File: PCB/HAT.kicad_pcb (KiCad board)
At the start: 2 copper layers, 99.4 x 99 mm, 103 parts, among them J1 Conn_01x02_Pin, J10 Conn_01x24_Socket, J11 Conn_01x24_Pin, J12 Conn_01x02_Pin, J13 Conn_01x02_Pin, J14 Conn_01x02_Pin, J15 Conn_01x02_Pin, J2 Conn_01x02_Pin, J3 Conn_01x01_Pin, J4 Conn_01x02_Pin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

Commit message: fixing of PCB Design
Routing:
- net GND: track 120.5 -> 126.1 mm
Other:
- board size 99.4 x 99 mm -> 99.3 x 98.9 mm
- board text added: "CHARGING MODULE"
- board text added: "CLOCK GENERATOR"
- board text added: "EEEPROM"
- board text added: "FTDI"
- board text added: "POLARITY PROTECTION + UVLO"
- board text added: "PROXIMITY SENSOR"
- board text added: "SHIFTER GPIO0"
- board text added: "SHIFTER GPIO1"
- board text added: "SHIFTER SCL"
- board text added: "SHIFTER SDA"
- board text added: "USB-B"
- board text added: "V REG"
- board text added: "VOLT REG SENSE"
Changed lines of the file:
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@@
         (effects (font (size 1 1) (thickness 0.15)))
     )
-    (fp_text user "REF**" (at 0 4.8 180) (layer "F.Fab")
-        (effects (font (size 1 1) (thickness 0.15)))
-    )
     (fp_line (start -0.9 -0.8) (end 0.9 -0.8)
-      (stroke (width 0.254001) (type solid)) (layer "F.SilkS"))
+      (stroke (width 0.254) (type solid)) (layer "F.SilkS"))
     (fp_line (start -0.878105 0.8) (end 0.878105 0.8)
-      (stroke (width 0.254001) (type solid)) (layer "F.SilkS"))
+      (stroke (width 0.254) (type solid)) (layer "F.SilkS"))
     (fp_line (start -0.609601 0) (end 0.685801 0)
       (stroke (width 0.2) (type solid)) (layer "F.SilkS"))
@@
     (fp_arc (start 1.080188 -0.709627) (mid 1.299286 -0.618875) (end 1.390018 -0.399772)
       (stroke (width 0.254) (type solid)) (layer "F.SilkS"))
-    (fp_arc (start 1.390018 0.400203) (mid 1.299269 0.61928) (end 1.080188 0.710033)
+    (fp_arc (start 1.390018 0.400203) (mid 1.299267 0.619284) (end 1.080188 0.710033)
       (stroke (width 0.254) (type solid)) (layer "F.SilkS"))
     (fp_circle (center -0.800102 0.400051) (end -0.77013 0.400051)
@@
     (fp_arc (start 1.080188 -0.709627) (mid 1.299286 -0.618875) (end 1.390018 -0.399772)
       (stroke (width 0.254) (type solid)) (layer "F.SilkS"))
-    (fp_arc (start 1.390018 0.400203) (mid 1.299269 0.61928) (end 1.080188 0.710033)
+    (fp_arc (start 1.390018 0.400203) (mid 1.299267 0.619284) (end 1.080188 0.710033)
       (stroke (width 0.254) (type solid)) (layer "F.SilkS"))
     (fp_circle (center -0.800102 0.400051) (end -0.77013 0.400051)
@@
     )
   )
-  (gr_rect (start 96.5964 46.9657) (end 195.5964 145.6449)
-    (stroke (width 0.2) (type default)) (fill none) (layer "F.Cu"))
+  (gr_circle (center 137.3378 101.6762) (end 137.5156 101.854)
+    (stroke (width 0.15) (type default)) (fill solid) (layer "F.SilkS"))
   (gr_rect (start 123.5964 68.6449) (end 172.6164 86.5999)
     (stroke (width 0.15) (type default)) (fill none) (layer "F.SilkS"))
@@
   (gr_rect (start 142.3964 115.069824) (end 157.2964 144.019824)
     (stroke (width 0.15) (type default)) (fill none) (layer "F.SilkS"))
+  (gr_circle (center 101.967847 69.8349) (end 102.145647 70.0127)
+    (stroke (width 0.15) (type default)) (fill solid) (layer "F.SilkS"))
   (gr_rect (start 173.0864 68.6449) (end 188.1064 86.5999)
     (stroke (width 0.15) (type default)) (fill none) (layer "F.SilkS"))
+  (gr_circle (center 172.443153 100.7872) (end 172.620953 100.965)
+    (stroke (width 0.15) (type default)) (fill solid) (layer "F.SilkS"))
   (gr_line (start 98.7964 129.6699) (end 113.6964 129.6699)
     (stroke (width 0.15) (type default)) (layer "F.SilkS"))
   (gr_rect (start 97.5964 68.6449) (end 122.6164 86.5999)
     (stroke (width 0.15) (type default)) (fill none) (layer "F.SilkS"))
+  (gr_rect (start 118.3386 127.2794) (end 139.065 145.5928)
+    (stroke (width 0.15) (type default)) (fill none) (layer "F.SilkS"))
   (gr_rect (start 161.6954 94.8279) (end 168.5534 105.2419)
     (stroke (width 0.15) (type default)) (fill none) (layer "F.SilkS"))
   (gr_rect (start 170.7124 88.4525) (end 185.4952 106.7405)
     (stroke (width 0.15) (type default)) (fill none) (layer "F.SilkS"))
-  (gr_rect (start 96.3412 46.7965) (end 195.7568 145.8057)
-    (stroke (width 0.1) (type default)) (fill none) (layer "Edge.Cuts"))
+  (gr_arc (start 97.399265 145.693738) (mid 96.731887 145.417111) (end 96.443801 144.7546)
+    (stroke (width 0.1) (type default)) (layer "Edge.Cuts"))
+  (gr_arc (start 195.707 144.78) (mid 195.386583 145.48655) (end 194.6666 145.775524)
+    (stroke (width 0.1) (type default)) (layer "Edge.Cuts"))
+  (gr_arc (start 96.443801 47.842944) (mid 96.729905 47.16669) (end 97.409 46.887396)
+    (stroke (width 0.1) (type default)) (layer "Edge.Cuts"))
+  (gr_line (start 97.409 46.887396) (end 194.705613 46.837601)
+    (stroke (width 0.1) (type default)) (layer "Edge.Cuts"))
+  (gr_line (start 96.443801 144.7546) (end 96.443801 47.842944)
+    (stroke (width 0.1) (type default)) (layer "Edge.Cuts"))
+  (gr_line (start 97.399265 145.693738) (end 194.6666 145.775524)
+    (stroke (width 0.1) (type default)) (layer "Edge.Cuts"))
+  (gr_line (start 195.725586 47.867228) (end 195.707 144.78)
+    (stroke (width 0.1) (type default)) (layer "Edge.Cuts"))
+  (gr_arc (start 194.705613 46.837601) (mid 195.427423 47.142577) (end 195.725586 47.867228)
+    (stroke (width 0.1) (type default)) (layer "Edge.Cuts"))
+  (gr_text "PROXIMITY SENSOR" (at 118.0084 143.6878 90) (layer "F.SilkS")
+    (effects (font (size 1 1) (thickness 0.15)) (justify left bottom))
+  )
+  (gr_text "SHIFTER GPIO1" (at 157.2964 115.069824 270) (layer "F.SilkS")
+    (effects (font (size 1 1) (thickness 0.15)) (justify left bottom))
+  )
+  (gr_text "V REG" (at 182.9054 71.0438) (layer "F.SilkS")
+    (effects (font (size 1 1) (thickness 0.15)) (justify left bottom))
+  )
+  (gr_text "FTDI" (at 187.1218 105.6894 90) (layer "F.SilkS")
+    (effects (font (size 1 1) (thickness 0.15)) (justify left bottom))
+  )
   (gr_text "EEE3088F GROUP 3\n" (at 170.8648 109.8393) (layer "F.SilkS")
     (effects (font (face "Arial") (size 1.5 1.5) (thickness 0.2) bold) (justify left bottom))
@@
     )
   )
+  (gr_text "EEEPROM" (at 145.0594 102.9716 90) (layer "F.SilkS")
+    (effects (font (size 1 1) (thickness 0.15)) (justify left bottom))
+  )
   (gr_text "Michael Awe AWXMIC001\nSimon Carthew CRTSIM008\nAdrian McIntosh MCNADR001" (at 180.8724 114.8177) (layer "F.SilkS")
     (effects (font (size 1 1) (thickness 0.15)) (justify bottom))
   )
+  (gr_text "SHIFTER SCL" (at 98.7964 129.6699 90) (layer "F.SilkS")
+    (effects (font (size 1 1) (thickness 0.15)) (justify left bottom))
+  )
+  (gr_text "POLARITY PROTECTION + UVLO" (at 135.3058 72.0852) (layer "F.SilkS")
+    (effects (font (size 1 1) (thickness 0.15)) (justify left bottom))
+  )
+  (gr_text "VOLT REG SENSE" (at 116.0964 127.0074 90) (layer "F.SilkS")
+    (effects (font (size 1 1) (thickness 0.15)) (justify left bottom))
+  )
+  (gr_text "SHIFTER GPIO0" (at 157.3276 131.318 270) (layer "F.SilkS")
+    (effects (font (size 1 1) (thickness 0.15)) (justify left bottom))
+  )
+  (gr_text "SHIFTER SDA" (at 98.7964 144.1449 90) (layer "F.SilkS")
+    (effects (font (size 1 1) (thickness 0.15)) (justify left bottom))
+  )
+  (gr_text "CLOCK GENERATOR" (at 122.8344 105.9942) (layer "F.SilkS")
+    (effects (font (size 1 1) (thickness 0.15)) (justify left bottom))
+  )
+  (gr_text "USB-B" (at 189.3824 91.3384) (layer "F.SilkS")
+    (effects (font (size 1 1) (thickness 0.15)) (justify left bottom))
+  )
+  (gr_text "CHARGING MODULE" (at 107.95 85.979) (layer "F.SilkS")
+    (effects (font (size 1 1) (thickness 0.15)) (justify left bottom))
+  )
   (segment (start 112.623 78.6715) (end 112.5964 78.6449) (width 1) (layer "F.Cu") (net 1))
   (segment (start 97.9668 89.8241) (end 97.8464 89.9445) (width 1) (layer "F.Cu") (net 1))
@@
   (segment (start 126.428745 130.269394) (end 126.428745 132.040849) (width 0.25) (layer "F.Cu") (net 2))
   (segment (start 136.038144 139.2149) (end 137.6664 139.2149) (width 1) (layer "F.Cu") (net 2))
+  (segment (start 151.578568 102.574897) (end 157.1234 102.574897) (width 0.6) (layer "F.Cu") (net 2))
   (segment (start 132.8964 134.995027) (end 132.8964 135.3449) (width 0.25) (layer "F.Cu") (net 2))
   (segment (start 105.1664 72.0399) (end 105.1664 72.3949) (width 1) (layer "F.Cu") (net 2))
@@
   (segment (start 137.1964 88.6149) (end 137.1764 88.5949) (width 0.6) (layer "F.Cu") (net 117))
   (zone (net 2) (net_name "GND") (layers "F&B.Cu") (hatch edge 0.5)
+    (priority 1)
     (connect_pads (clearance 0.5))
     (min_thickness 0.25) (filled_areas_thickness no)
@@
     (polygon
       (pts
-        (xy 96.5964 46.9657)
-        (xy 96.5964 145.6449)
-        (xy 195.5964 145.6449)
-        (xy 195.5964 46.9657)
+        (xy 96.5454 49.9618)
+        (xy 99.314 47.0662)
+        (xy 193.6242 47.0916)
+        (xy 195.453 49.022)
+        (xy 195.6308 143.7132)
+        (xy 193.802 145.6182)
+        (xy 97.8154 145.5674)
+        (xy 96.5962 144.5006)
       )
     )

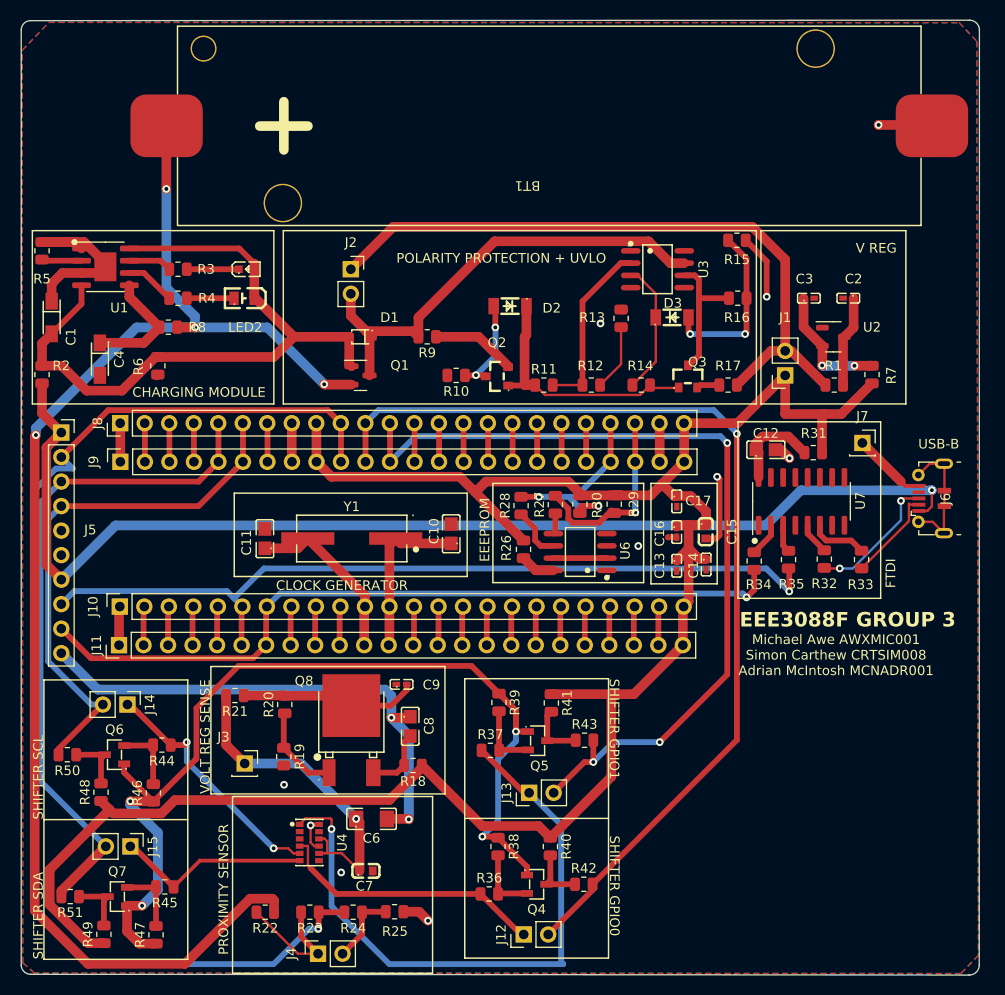
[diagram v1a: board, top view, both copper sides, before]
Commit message: Pins not Sockets
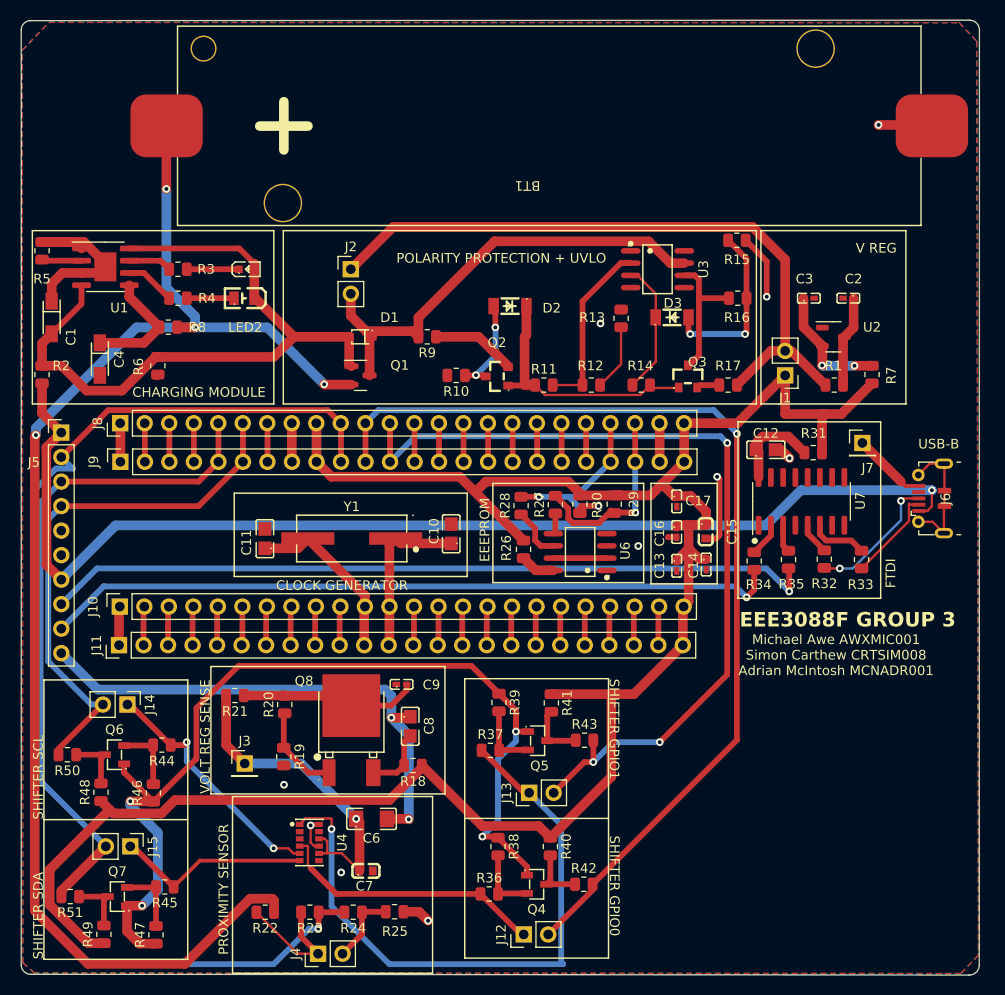
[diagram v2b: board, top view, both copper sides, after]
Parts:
- J1, J2, J4: footprint Connector_PinSocket_2.54mm:PinSocket_1x02_P2.54mm_Vertical -> Connector_PinHeader_2.54mm:PinHeader_1x02_P2.54mm_Vertical
- J3, J7: footprint Connector_PinSocket_2.54mm:PinSocket_1x01_P2.54mm_Vertical -> Connector_PinHeader_2.54mm:PinHeader_1x01_P2.54mm_Vertical
- J5: footprint Connector_PinSocket_2.54mm:PinSocket_1x10_P2.54mm_Vertical -> Connector_PinHeader_2.54mm:PinHeader_1x10_P2.54mm_Vertical
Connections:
- J10 pad 6: USART_TX -> Net-(J10-Pin_6)
- J10 pad 7: USART_RX -> Net-(J10-Pin_7)
- J11 pad 6: USART_TX -> Net-(J10-Pin_6)
- J11 pad 7: USART_RX -> Net-(J10-Pin_7)
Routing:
- net USART_TX: track 86.2 -> 80.4 mm
- net USART_RX: track 80.7 -> 76.5 mm
- net Net-(J10-Pin_7): track 0.00 -> 4.03 mm
- net Net-(J10-Pin_6): track 0.00 -> 4.03 mm

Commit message: Final Fixes
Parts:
- added D4: D_Schottky, JLC_Diodes:SOD-323_L1.8-W1.3-LS2.5-RD, F.Cu at (126.8, 84.7)
- moved BT1 3.16 mm to (148.0, 57.2)
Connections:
- Q1 pad 2: /Power Module/V_BAT+ -> Net-(D4-K)
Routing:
- net Net-(D4-K): track 0.00 -> 2.73 mm
- net /Power Module/V_BAT+: track 144.7 -> 142.2 mm
- net /MicroController_Interfacing/3V3: track 220.9 -> 219.1 mm
- net GND: track 126.1 -> 127.6 mm
- net /Power Module/UVLO_3V3: track 69.8 -> 70.8 mm
- net /Power Module/CHRG_OUT: track 48.9 -> 49.5 mm
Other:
- board size 99.3 x 98.9 mm -> 97.6 x 98.9 mm
